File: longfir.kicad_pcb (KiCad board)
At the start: 2 copper layers, 140.5 x 99.1 mm, 34 parts, among them J1 MJ-4PP-9, K1 diode-choc, K10 diode-choc, K11 diode-choc, K12 diode-choc, K13 diode-choc, K14 diode-choc, K15 diode-choc, K16 diode-choc, K17 diode-choc, K18 diode-choc, K19 diode-choc, K2 diode-choc, K20 diode-choc, K21 diode-choc, K22 diode-choc, K23 diode-choc, K24 diode-choc, K3 diode-choc, K4 diode-choc, K5 diode-choc, K6 diode-choc, K7 diode-choc, K8 diode-choc, K9 diode-choc, SW1 SW_PUSH, U1 ProMicro_r

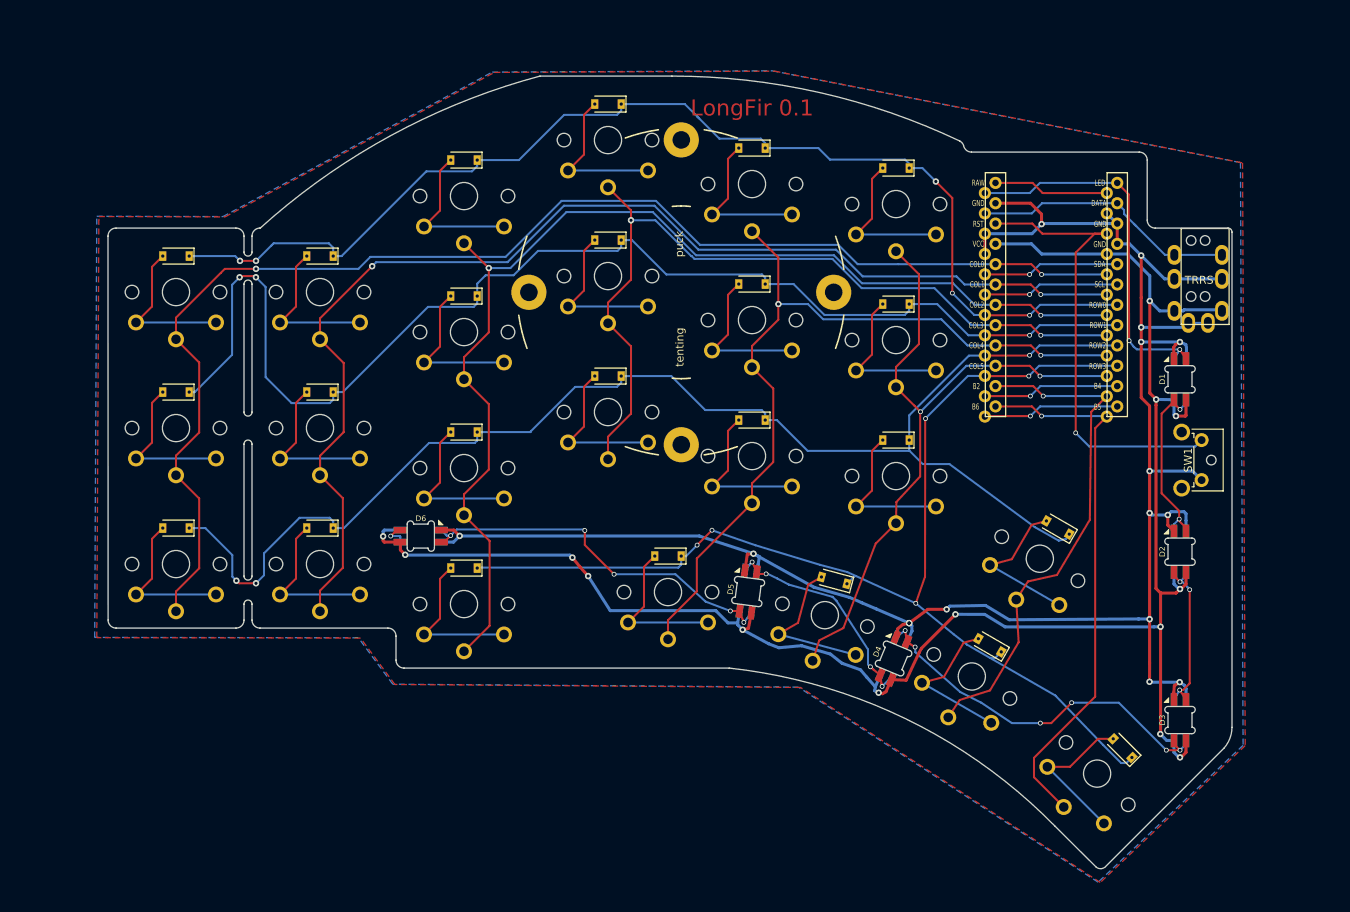
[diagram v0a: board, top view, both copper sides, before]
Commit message: Remove acid traps
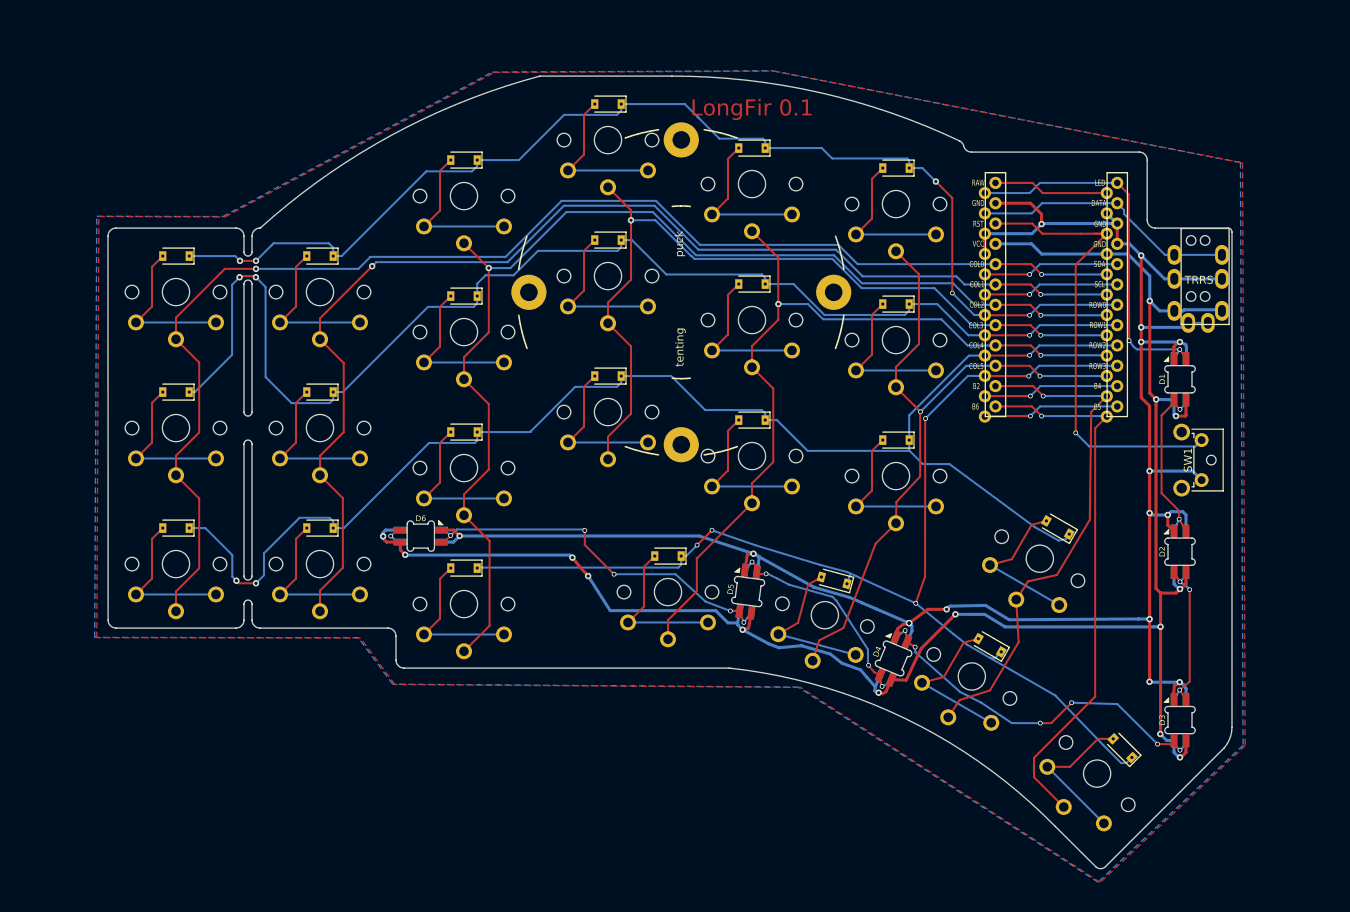
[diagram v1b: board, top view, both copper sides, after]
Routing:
- net reset: track 58.6 -> 59.2 mm

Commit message: Fix switch footprint traces, Fix Tenting Puck
Footprints:
- Choc-diode traces as lines not custom pads, so show in gerber; diode silk end bar further from pad and mask
- Tenting Puck screws better clearance
- Move board label to lower center
- LEDs Ref# on fabrication layer, not silk
- Rewire TRRS to work with TRS cables

- TRRS moved in and up more
- Smoother curve on lower left edge cut

- Pads for haptic header
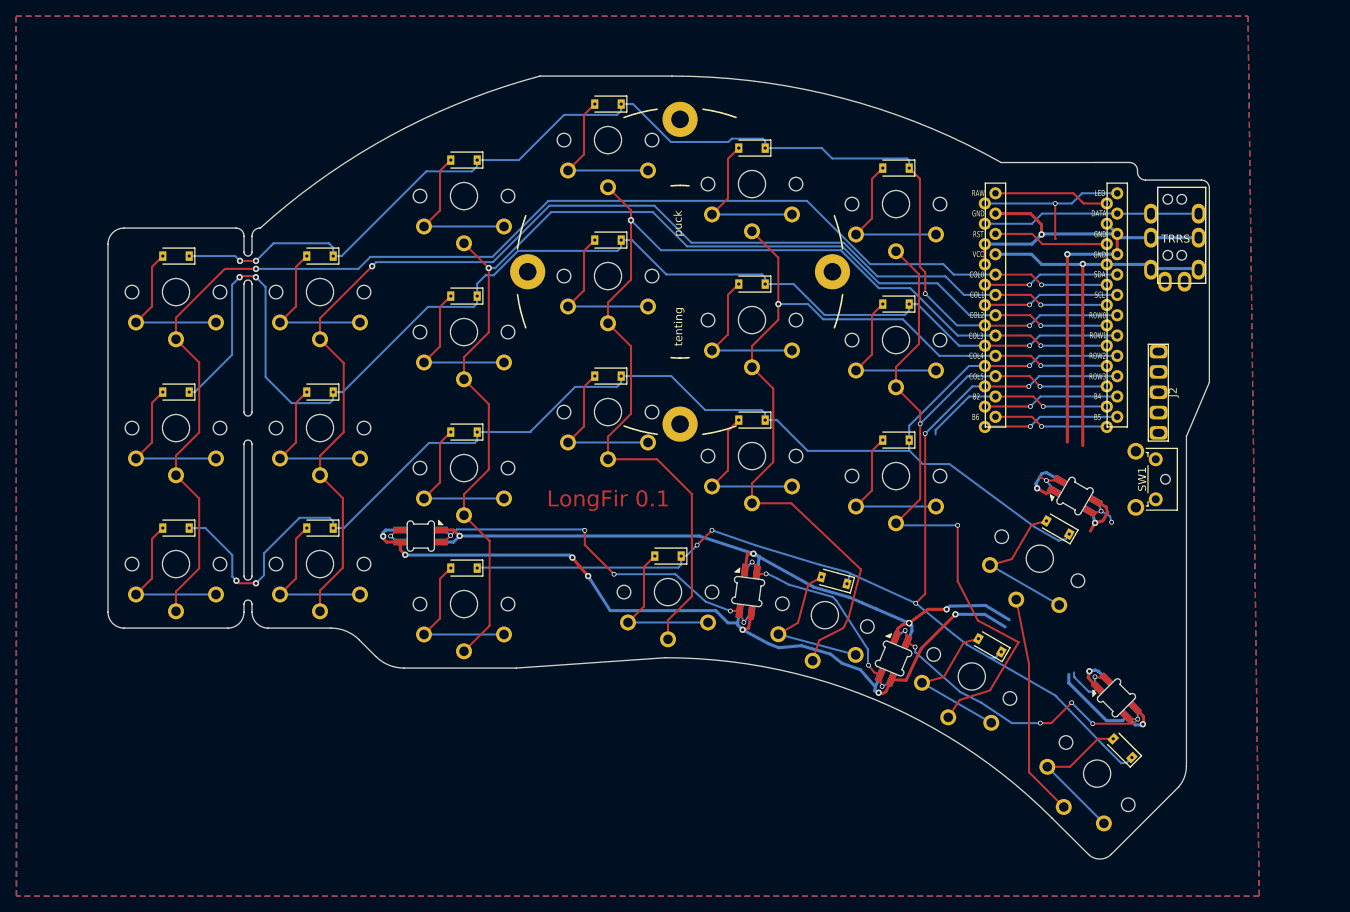
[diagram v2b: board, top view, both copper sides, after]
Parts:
- removed the D1 at (225.5, 95.4)
- removed the D3 at (225.5, 138.0)
- added D2: SK6812-MINI-E, longfir:SK6812-MINI-E, F.Cu at (217.6, 135.2)
- added J2: Conn_01x05-Connector_Generic, mmccoyd:pimoroni_left_side_mount, F.Cu at (223.0, 97.0)
- K1, K10, K11, K12, K13, K14, K15, K16, K17, K18, K19, K2, K20, K21, K22, K23, K24, K3, K4, K5, K6, K7, K8, K9: footprint longfir:pg1350-DR -> cridesgit:pg1350-DR
- moved D1 14.8 mm to (212.4, 110.0), turned to 150 degrees
- moved SW1 6.21 mm to (222.5, 105.4)
- moved J1 5.92 mm to (225.7, 71.4)
- moved REF** 2.57 mm to (163.0, 82.0)
- moved U1 1.30 mm to (210.0, 86.6)
- renumbered D2 to D1, D4 to D3, D5 to D4, D6 to D5
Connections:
- D1 pad 4: Net-(D1-Pad2) (its old number) -> LED
- J1 pad A: GND -> Net-(J1-PadA)
- K21 pad 1: col4 -> col3
- K22 pad 1: col5 -> col4
- K23 pad 1: col6 -> col5
- K24 pad 1: col7 -> col6
- U1 pad 12: Net-(U1-Pad12) -> trig
- U1 pad 13: col7 -> Net-(U1-Pad13)
- U1 pad 5: Net-(U1-Pad5) -> SDA
- U1 pad 6: Net-(U1-Pad6) -> SCL
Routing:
- net GND: track 250.0 -> 172.3 mm, vias 16 -> 9
- net col7: track 68.6 -> 0.00 mm, vias 1 -> 0
- net VCC: track 231.9 -> 173.2 mm, vias 14 -> 10
- net reset: track 59.2 -> 16.0 mm, vias 1 -> 0
- net col3: track 104.2 -> 136.4 mm
- net Net-(D1-Pad2) (its old number): track 22.9 -> 0.00 mm, vias 2 -> 0
- net LED: track 47.0 -> 26.0 mm
- net col5: track 86.0 -> 104.9 mm, vias 2 -> 3
- net SDA: track 0.00 -> 17.1 mm, vias 0 -> 1
- net Net-(U1-Pad5): track 17.1 -> 0.00 mm, vias 1 -> 0
- net trig: track 0.00 -> 17.1 mm, vias 0 -> 1
- net Net-(U1-Pad12): track 17.1 -> 0.00 mm, vias 1 -> 0
- net SCL: track 0.00 -> 17.1 mm, vias 0 -> 1
- net Net-(U1-Pad6): track 17.1 -> 0.00 mm, vias 1 -> 0
- net Net-(U1-Pad13): track 0.00 -> 14.4 mm, vias 0 -> 1
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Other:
- board size 140.5 x 99.1 mm -> 137.7 x 97.9 mm

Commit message: Use 6 columns. Bottom row traces run two cols over
- LEDs tucked under top edge of bottom row keys.
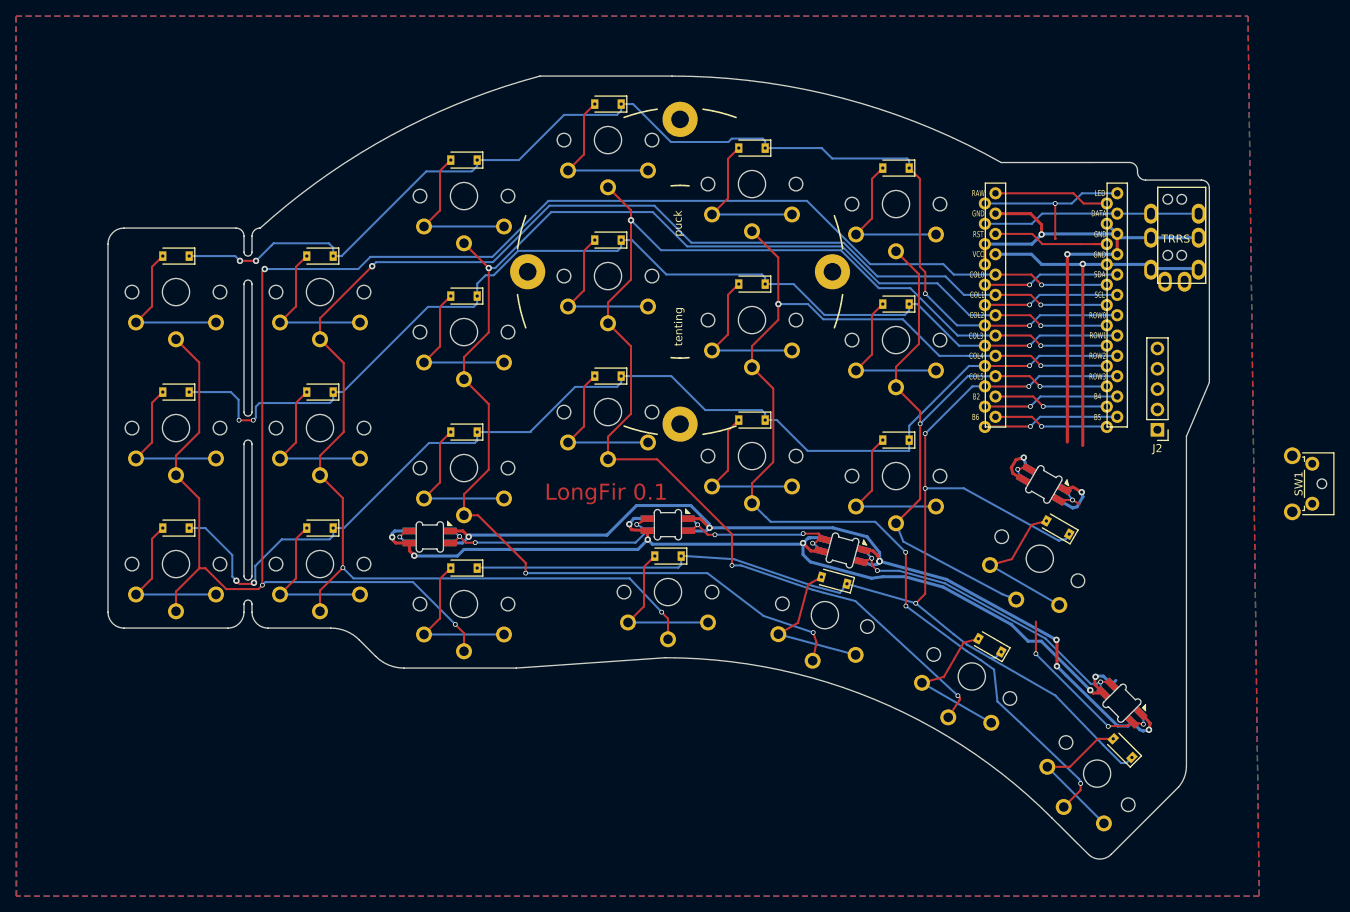
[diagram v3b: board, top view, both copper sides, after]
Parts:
- J2: value Conn_01x05-Connector_Generic -> HapticHeader; footprint mmccoyd:pimoroni_left_side_mount -> longfir:HapticHeader_1x05
- moved SW1 19.6 mm to (242.0, 106.0)
- moved D3 14.9 mm to (183.3, 116.8), turned to 345 degrees
- moved D4 13.1 mm to (161.5, 113.6), turned to 0 degrees
- moved J2 4.75 mm to (222.7, 101.7), turned to 180 degrees
- moved D1 4.16 mm to (208.5, 108.5), turned to 330 degrees
- moved D5 1.14 mm to (131.7, 115.1)
- moved D2 0.96 mm to (218.2, 135.9), turned to 315 degrees
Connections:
- K19 pad 1: col6 -> col5
- K19 pad 2: row2 -> row3
- K20 pad 1: col2 -> col0
- K21 pad 1: col3 -> col1
- K22 pad 1: col4 -> col2
- K23 pad 1: col5 -> col3
- K24 pad 1: col6 -> col4
- U1 pad 14: col6 -> Net-(U1-Pad14)
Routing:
- net col0: track 168.3 -> 231.1 mm, vias 2 -> 4
- net col6: track 52.1 -> 0.00 mm, vias 1 -> 0
- net col1: track 150.8 -> 196.7 mm, vias 2 -> 4
- net col4: track 113.9 -> 147.8 mm, vias 2 -> 5
- net col2: track 144.8 -> 178.4 mm, vias 2 -> 4
- net col3: track 136.4 -> 164.8 mm, vias 2 -> 4
- net row2: track 170.6 -> 145.2 mm
- net GND: track 172.3 -> 197.3 mm, vias 9 -> 10
- net col5: track 104.9 -> 83.9 mm, vias 3 -> 2
- net row1: track 159.3 -> 140.4 mm
- net row3: track 145.2 -> 162.5 mm, vias 5 -> 4
- net Net-(D4-Pad2): track 47.4 -> 30.5 mm, vias 5 -> 3
- net Net-(U1-Pad14): track 0.00 -> 14.4 mm, vias 0 -> 1
- net Net-(D1-Pad2): track 12.6 -> 26.1 mm, vias 3 -> 4
- net Net-(D3-Pad2): track 27.9 -> 23.1 mm
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
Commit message: Pull up resistors for I2C
- Use bottom plate as ground plate
- Sym Diode-Choc: suppress pin numbers in schematic
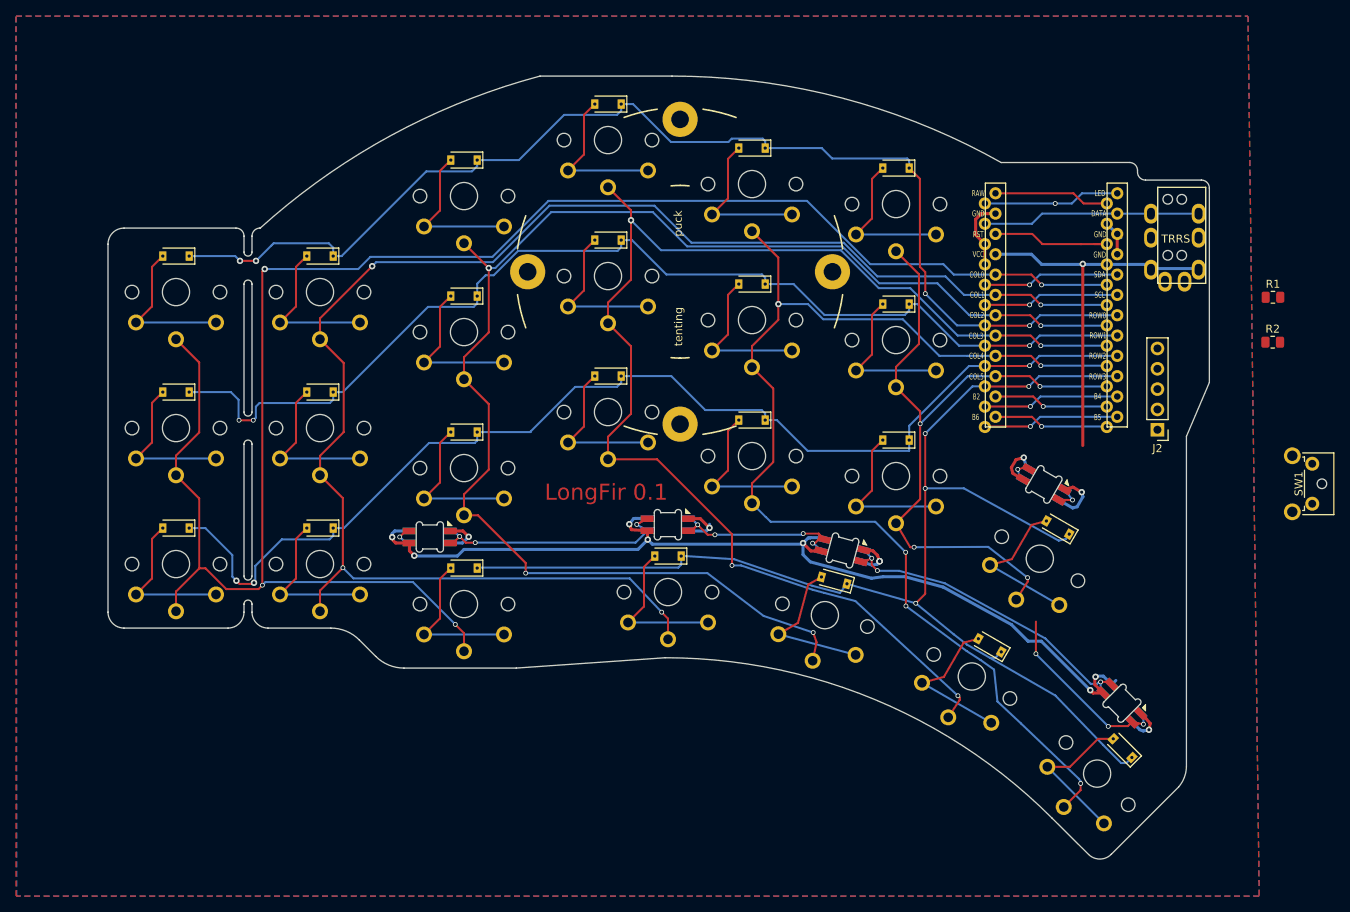
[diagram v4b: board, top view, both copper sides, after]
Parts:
- added R1: R, ki_resist_smd:R_0805_2012Metric, F.Cu at (237.1, 85.2)
- added R2: R, ki_resist_smd:R_0805_2012Metric, F.Cu at (237.1, 90.8)
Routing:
- net GND: track 197.3 -> 43.1 mm, vias 10 -> 6
- net LED: track 26.0 -> 20.5 mm
- net col5: track 83.9 -> 88.2 mm, vias 2 -> 4
- added copper zone on B.Cu, net GND
- removed copper zone on B.Cu, net (none)

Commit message: PCB: Haptic, TRRS, reset angled, smooth edge cuts
- Haptic on side
- Reset angled
- Trace cleanup
- Edge cuts smooth
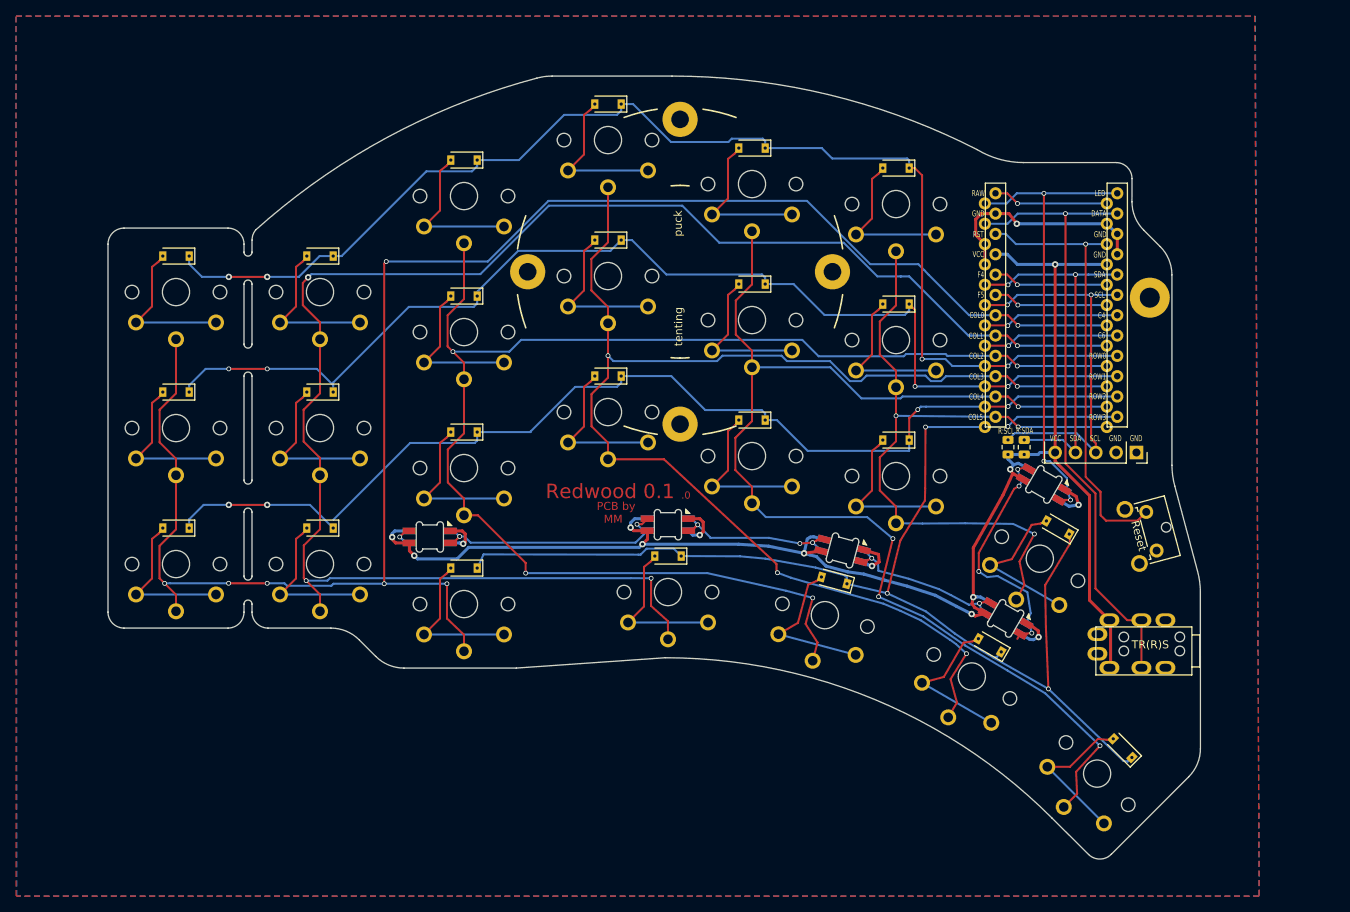
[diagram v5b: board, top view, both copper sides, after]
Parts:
- J1: value MJ-4PP-9 -> Haptic; footprint kbd:MJ-4PP-9 -> longfir:PomoroniHaptic
- J2: value HapticHeader -> TRRS; footprint longfir:HapticHeader_1x05 -> longfir:MJ-4PP-9
- K1, K10, K11, K12, K13, K14, K15, K16, K17, K18, K19, K2, K20, K21, K22, K23, K24, K3, K4, K5, K6, K7, K8, K9: footprint cridesgit:pg1350-DR -> longfir:pg1350-DR
- R1: value R -> R:SCL; footprint ki_resist_smd:R_0805_2012Metric -> longfir:R_0805_2012Metric_DoubleSided
- R2: value R -> R:SDA; footprint ki_resist_smd:R_0805_2012Metric -> longfir:R_0805_2012Metric_DoubleSided
- SW1: value SW_PUSH -> Reset; footprint keebio:SW_Tactile_SPST_Angled_MJTP1117 -> longfir:SW_Tactile_SPST_Angled_MJTP1117
- U1: footprint kbd:ProMicro_v2 -> longfir:ProMicro_v2
- moved R1 38.1 mm to (204.0, 103.9), turned to 90 degrees
- moved R2 33.7 mm to (206.0, 103.9), turned to 90 degrees
- moved J2 28.7 mm to (215.0, 129.4), turned to 90 degrees
- moved J1 24.5 mm to (215.0, 93.5)
- moved SW1 21.6 mm to (221.3, 112.0), turned to 285 degrees
- moved D2 18.0 mm to (203.7, 125.3), turned to 330 degrees
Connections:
- R1 pad 2: SDA -> SCL
- R2 pad 2: SCL -> SDA
- U1 pad 10: row3 -> row1
- U1 pad 11: Net-(U1-Pad11) -> row2
- U1 pad 12: trig -> row3
- U1 pad 13: Net-(U1-Pad13) -> col5
- U1 pad 14: Net-(U1-Pad14) -> col4
- U1 pad 15: col5 -> col3
- U1 pad 16: col4 -> col2
- U1 pad 17: col3 -> col1
- U1 pad 18: col2 -> col0
- U1 pad 19: col1 -> Net-(U1-Pad19)
- U1 pad 20: col0 -> Net-(U1-Pad20)
- U1 pad 7: row0 -> Net-(U1-Pad7)
- U1 pad 8: row1 -> Net-(U1-Pad8)
- U1 pad 9: row2 -> row0
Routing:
- net data: track 27.2 -> 78.8 mm, vias 0 -> 1
- net reset: track 16.0 -> 55.5 mm, vias 0 -> 1
- net LED: track 20.5 -> 58.9 mm, vias 2 -> 3
- net SCL: track 17.1 -> 49.3 mm, vias 1 -> 2
- net SDA: track 17.1 -> 46.4 mm, vias 1 -> 2
- net VCC: track 174.6 -> 197.0 mm
- net Net-(D2-Pad2): track 40.1 -> 21.4 mm, vias 3 -> 2
- net Net-(U1-Pad7): track 0.00 -> 17.1 mm, vias 0 -> 1
- net Net-(U1-Pad11): track 17.1 -> 0.00 mm, vias 1 -> 0
- net trig: track 17.1 -> 0.00 mm, vias 1 -> 0
- net Net-(U1-Pad8): track 0.00 -> 17.1 mm, vias 0 -> 1
- net Net-(U1-Pad13): track 14.4 -> 0.00 mm, vias 1 -> 0
- net Net-(U1-Pad20): track 0.00 -> 14.4 mm, vias 0 -> 1
- net Net-(U1-Pad19): track 0.00 -> 14.4 mm, vias 0 -> 1
- net Net-(U1-Pad14): track 14.4 -> 0.00 mm, vias 1 -> 0
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- added copper zone on F.Cu, net GND
- removed copper zone on F.Cu, net (none)
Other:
- board size 137.7 x 97.9 mm -> 136.6 x 97.9 mm
- board text added: ".0"
- board text added: "PCB by MM"
- board text added: "Redwood 0.1"
- board text removed: "LongFir 0.1"
